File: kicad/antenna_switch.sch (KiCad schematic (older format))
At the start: 138 parts, among them K1 Fujitsu_FTR-K1C, K10 Fujitsu_FTR-K1C, K11 Fujitsu_FTR-K1C, K12 Fujitsu_FTR-K1C, K13 Fujitsu_FTR-K1C, K14 Fujitsu_FTR-K1C, K15 Fujitsu_FTR-K1C, K16 Fujitsu_FTR-K1C, K17 Fujitsu_FTR-K1C, K18 Fujitsu_FTR-K1C, K19 Fujitsu_FTR-K1C, K2 Fujitsu_FTR-K1C, K20 Fujitsu_FTR-K1C, K3 Fujitsu_FTR-K1C, K4 Fujitsu_FTR-K1C, K5 Fujitsu_FTR-K1C, K6 Fujitsu_FTR-K1C, K7 Fujitsu_FTR-K1C, K8 Fujitsu_FTR-K1C, K9 Fujitsu_FTR-K1C, Q1 BSS138, Q10 BSS138, Q11 BSS138, Q12 BSS138, Q13 BSS138, Q14 BSS138, Q15 BSS138, Q16 BSS138, Q17 BSS138, Q18 BSS138, Q19 BSS138, Q2 BSS138, Q20 BSS138, Q3 BSS138, Q4 BSS138, Q5 BSS138, Q6 BSS138, Q7 BSS138, Q8 BSS138, Q9 BSS138, U1 7400, U2 7400, U3 7400, U4 7400, U5 7400, U6 7400, U7 7400, U8 7400

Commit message: Schematic libs
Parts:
- K1, K10, K11, K12, K13, K14, K15, K16, K17, K18, K19, K2, K20, K3, K4, K5, K6, K7, K8, K9: symbol antenna_switch-rescue:Fujitsu_FTR-K1C-QS_RF -> antenna_switch:Fujitsu_FTR-K1C
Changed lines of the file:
@@
 $EndDescr
 $Comp
-L antenna_switch-rescue:Fujitsu_FTR-K1C-QS_RF K1
+L antenna_switch:Fujitsu_FTR-K1C K1
 U 1 1 5D35D937
 P 2750 1750
@@
 	2350 2100 2350 2150
 $Comp
-L antenna_switch-rescue:Fujitsu_FTR-K1C-QS_RF K2
+L antenna_switch:Fujitsu_FTR-K1C K2
 U 1 1 5D37821A
 P 2750 3800
@@
 	2350 4150 2350 4200
 $Comp
-L antenna_switch-rescue:Fujitsu_FTR-K1C-QS_RF K3
+L antenna_switch:Fujitsu_FTR-K1C K3
 U 1 1 5D37A38D
 P 2750 5900
@@
 	2000 6500 1950 6500
 $Comp
-L antenna_switch-rescue:Fujitsu_FTR-K1C-QS_RF K4
+L antenna_switch:Fujitsu_FTR-K1C K4
 U 1 1 5D3DAF7C
 P 4450 1750
@@
 	4050 2100 4050 2150
 $Comp
-L antenna_switch-rescue:Fujitsu_FTR-K1C-QS_RF K5
+L antenna_switch:Fujitsu_FTR-K1C K5
 U 1 1 5D3DAFB0
 P 4450 3800
@@
 	4050 4150 4050 4200
 $Comp
-L antenna_switch-rescue:Fujitsu_FTR-K1C-QS_RF K6
+L antenna_switch:Fujitsu_FTR-K1C K6
 U 1 1 5D3DAFD8
 P 4450 5900
@@
 	3700 6500 3650 6500
 $Comp
-L antenna_switch-rescue:Fujitsu_FTR-K1C-QS_RF K7
+L antenna_switch:Fujitsu_FTR-K1C K7
 U 1 1 5D3EC9E1
 P 6150 1750
@@
 	5750 2100 5750 2150
 $Comp
-L antenna_switch-rescue:Fujitsu_FTR-K1C-QS_RF K8
+L antenna_switch:Fujitsu_FTR-K1C K8
 U 1 1 5D3ECA15
 P 6150 3800
@@
 	5750 4150 5750 4200
 $Comp
-L antenna_switch-rescue:Fujitsu_FTR-K1C-QS_RF K9
+L antenna_switch:Fujitsu_FTR-K1C K9
 U 1 1 5D3ECA3D
 P 6150 5900
@@
 	5400 6500 5350 6500
 $Comp
-L antenna_switch-rescue:Fujitsu_FTR-K1C-QS_RF K10
+L antenna_switch:Fujitsu_FTR-K1C K10
 U 1 1 5D437770
 P 7850 1750
@@
 	7450 2100 7450 2150
 $Comp
-L antenna_switch-rescue:Fujitsu_FTR-K1C-QS_RF K11
+L antenna_switch:Fujitsu_FTR-K1C K11
 U 1 1 5D4377A4
 P 7850 3800
@@
 	7450 4150 7450 4200
 $Comp
-L antenna_switch-rescue:Fujitsu_FTR-K1C-QS_RF K12
+L antenna_switch:Fujitsu_FTR-K1C K12
 U 1 1 5D4377CC
 P 7850 5900
@@
 	7100 6500 7050 6500
 $Comp
-L antenna_switch-rescue:Fujitsu_FTR-K1C-QS_RF K13
+L antenna_switch:Fujitsu_FTR-K1C K13
 U 1 1 5D437834
 P 9550 1750
@@
 	9150 2100 9150 2150
 $Comp
-L antenna_switch-rescue:Fujitsu_FTR-K1C-QS_RF K14
+L antenna_switch:Fujitsu_FTR-K1C K14
 U 1 1 5D437868
 P 9550 3800
@@
 	9150 4150 9150 4200
 $Comp
-L antenna_switch-rescue:Fujitsu_FTR-K1C-QS_RF K15
+L antenna_switch:Fujitsu_FTR-K1C K15
 U 1 1 5D437890
 P 9550 5900
@@
 	8800 6500 8750 6500
 $Comp
-L antenna_switch-rescue:Fujitsu_FTR-K1C-QS_RF K16
+L antenna_switch:Fujitsu_FTR-K1C K16
 U 1 1 5D4378F8
 P 11250 1750
@@
 	10850 2100 10850 2150
 $Comp
-L antenna_switch-rescue:Fujitsu_FTR-K1C-QS_RF K17
+L antenna_switch:Fujitsu_FTR-K1C K17
 U 1 1 5D43792C
 P 11250 3800
@@
 	10850 4150 10850 4200
 $Comp
-L antenna_switch-rescue:Fujitsu_FTR-K1C-QS_RF K18
+L antenna_switch:Fujitsu_FTR-K1C K18
 U 1 1 5D437954
 P 11250 5900
@@
 $EndComp
 $Comp
-L antenna_switch-rescue:Fujitsu_FTR-K1C-QS_RF K19
+L antenna_switch:Fujitsu_FTR-K1C K19
 U 1 1 5D67F737
 P 12750 2350
@@
 Connection ~ 11400 3050
 $Comp
-L antenna_switch-rescue:Fujitsu_FTR-K1C-QS_RF K20
+L antenna_switch:Fujitsu_FTR-K1C K20
 U 1 1 5DD9CFD4
 P 12750 4650

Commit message: Compensation coils
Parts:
- added L1, L2: L, symbol Device:L
- gave numbers to parts that had none: 8
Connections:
- wire segments 530 -> 532

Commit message: Relays in series to increase isolation
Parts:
- removed C8: 100n, symbol Device:C_Small
- removed D10, D11, D12, D14, D15, D16, D4, D6, D7, D8, D9: 1N4148WS, Diode_SMD:D_SOD-323, symbol Diode:1N4148WS
- removed EXT1, EXT2, LOAD1, LOAD2, RADIO1, RADIO2: Conn_Coaxial, symbol Connector:Conn_Coaxial
- removed K19, K20, K4, K6: Fujitsu_FTR-K1C, QS_RF:Relay_DPDT_Fujitsu_FTR-K1C, symbol antenna_switch:Fujitsu_FTR-K1C
- removed L1, L2: L, symbol Device:L
- removed Q1, Q10, Q11, Q12, Q13, Q14, Q15, Q16, Q17, Q18, Q19, Q2, Q20, Q3, Q4, Q5, Q6, Q7, Q8, Q9: BSS138, Package_TO_SOT_SMD:SOT-23, symbol Transistor_FET:BSS138
- removed R1, R10, R11, R12, R13, R14, R15, R16, R17, R18, R19, R2, R20, R3, R4, R5, R6, R7, R8, R9: 470k, symbol Device:R_Small
- removed U1, U10, U11, U12, U13, U14, U15, U16, U2, U3, U4, U5, U6, U7, U8, U9: 7400, symbol 74xx:7400
- added C10, C11, C12, C13, C14, C9: 1n, symbol Device:C_Small
- added C8: 470u, symbol Device:CP_Small
- added D1, D10, D15, D16, D2, D24, D25, D30, D31, D38, D39, D9: CGA0603MLC-12E, symbol Device:D_TVS
- added D11, D12, D21, D22, D23, D26, D27, D36, D37, D40, D41, D7, D8: LED, symbol Device:LED
- added D28, D29, D3, D32, D33, D34, D35, D42, D43: 1N4148WS, Diode_SMD:D_SOD-323, symbol Diode:1N4148WS
- added E1, E10, E13, E14, E15, E16, E17, E2, E3, E4, E7, E8, E9: CG775MS, symbol Device:SPARK_GAP
- added E11, E12, E18, E19, E5, E6: SL1002A600SM, symbol Device:SPARK_GAP
- added J1: Conn_02x07_Odd_Even, symbol Connector_Generic:Conn_02x07_Odd_Even
- added J2: Conn_01x02, symbol Connector_Generic:Conn_01x02
- added K1, K3: Fujitsu_FTR-K1C, QS_RF:Relay_DPDT_Fujitsu_FTR-K1C, symbol antenna_switch:Fujitsu_FTR-K1C
- added L1, L2: L_Small, symbol Device:L_Small
- added Q1, Q10, Q11, Q12, Q2, Q3, Q4, Q5, Q6, Q7, Q8, Q9: BC817, Package_TO_SOT_SMD:SOT-23, symbol Transistor_BJT:BC817
- added R1, R10, R13, R14, R2, R22, R23, R26, R27, R34, R35, R9: 1k, symbol Device:R
- added R11, R12, R19, R20, R21, R24, R25, R32, R33, R36, R37, R7, R8: 4.7k, symbol Device:R
- added R15, R16, R17, R18, R28, R29, R3, R30, R31, R4, R5, R6: 100, symbol Device:R
- added TRX1, TRX2: Conn_Coaxial, symbol Connector:Conn_Coaxial
- C1, C2, C3, C4, C5, C6: value 100n -> 1n
- renumbered D3 to D14, D2 to D4, D1 to D6, K1 to K4, K3 to K6
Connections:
- net labels added: RADIO_1, RADIO_2
- net labels removed: Rel_A1G, Rel_A1R1, Rel_A1R2, Rel_A2G, Rel_A2R1, Rel_A2R2, Rel_A3G, Rel_A3R1, Rel_A3R2, Rel_A4G, Rel_A4R1, Rel_A4R2, Rel_A5G, Rel_A5R1, Rel_A5R2, Rel_A6G, Rel_A6R1, Rel_A6R2, Rel_R1L, Rel_R2L
- wire segments 532 -> 459
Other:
- moved on the sheet: A1, D14, D4, D6, K2, K4, K6

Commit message: Initial PCB layout work
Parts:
- removed E1, E10, E13, E14, E15, E16, E17, E2, E3, E4, E9: CG775MS, symbol Device:SPARK_GAP
- added D30: TESDU24V, Resistor_SMD:R_0603_1608Metric_Pad1.05x0.95mm_HandSolder, symbol Device:D_TVS
- added F1: 0ZCJ0025AF2E, Fuse:Fuse_1206_3216Metric_Pad1.42x1.75mm_HandSolder, symbol Device:Polyfuse_Small
- A1, A2, A3, A4, A5, A6, TRX1, TRX2: footprint (none) -> QS_RF:UC1-Square-2HolesRight
- C1: renamed from C2; footprint (none) -> Capacitor_SMD:C_0805_2012Metric_Pad1.15x1.40mm_HandSolder
- C10: renamed from C9; footprint (none) -> Capacitor_SMD:C_0805_2012Metric_Pad1.15x1.40mm_HandSolder
- C11: renamed from C12; footprint (none) -> Capacitor_SMD:C_0805_2012Metric_Pad1.15x1.40mm_HandSolder
- C12: renamed from C11; footprint (none) -> Capacitor_SMD:C_0805_2012Metric_Pad1.15x1.40mm_HandSolder
- C13: renamed from C14; footprint (none) -> Capacitor_SMD:C_0805_2012Metric_Pad1.15x1.40mm_HandSolder
- C14: renamed from C13; footprint (none) -> Capacitor_SMD:C_0805_2012Metric_Pad1.15x1.40mm_HandSolder
- C2: renamed from C1; footprint (none) -> Capacitor_SMD:C_0805_2012Metric_Pad1.15x1.40mm_HandSolder
- C3: renamed from C4; footprint (none) -> Capacitor_SMD:C_0805_2012Metric_Pad1.15x1.40mm_HandSolder
- C4: renamed from C3; footprint (none) -> Capacitor_SMD:C_0805_2012Metric_Pad1.15x1.40mm_HandSolder
- C5: renamed from C6; footprint (none) -> Capacitor_SMD:C_0805_2012Metric_Pad1.15x1.40mm_HandSolder
- C6: renamed from C5; footprint (none) -> Capacitor_SMD:C_0805_2012Metric_Pad1.15x1.40mm_HandSolder
- C7: footprint (none) -> Capacitor_SMD:C_0805_2012Metric_Pad1.15x1.40mm_HandSolder
- C8: footprint (none) -> Capacitor_THT:CP_Radial_D8.0mm_P3.50mm
- C9: renamed from C10; footprint (none) -> Capacitor_SMD:C_0805_2012Metric_Pad1.15x1.40mm_HandSolder
- D1: renamed from D2; value CGA0603MLC-12E -> TESDU24V; footprint (none) -> Resistor_SMD:R_0603_1608Metric_Pad1.05x0.95mm_HandSolder
- D10: renamed from D9; value CGA0603MLC-12E -> TESDU24V; footprint (none) -> Resistor_SMD:R_0603_1608Metric_Pad1.05x0.95mm_HandSolder
- D11: renamed from D12; footprint (none) -> LED_SMD:LED_0805_2012Metric_Pad1.15x1.40mm_HandSolder
- D12: renamed from D11; footprint (none) -> LED_SMD:LED_0805_2012Metric_Pad1.15x1.40mm_HandSolder
- D15: renamed from D16; value CGA0603MLC-12E -> TESDU24V; footprint (none) -> Resistor_SMD:R_0603_1608Metric_Pad1.05x0.95mm_HandSolder
- D16: renamed from D15; value CGA0603MLC-12E -> TESDU24V; footprint (none) -> Resistor_SMD:R_0603_1608Metric_Pad1.05x0.95mm_HandSolder
- D2: renamed from D1; value CGA0603MLC-12E -> TESDU24V; footprint (none) -> Resistor_SMD:R_0603_1608Metric_Pad1.05x0.95mm_HandSolder
- D21: renamed from D22; footprint (none) -> LED_SMD:LED_0805_2012Metric_Pad1.15x1.40mm_HandSolder
- D22: renamed from D21; footprint (none) -> LED_SMD:LED_0805_2012Metric_Pad1.15x1.40mm_HandSolder
- D23, D37, D41: footprint (none) -> LED_SMD:LED_0805_2012Metric_Pad1.15x1.40mm_HandSolder
- D24: renamed from D25; value CGA0603MLC-12E -> TESDU24V; footprint (none) -> Resistor_SMD:R_0603_1608Metric_Pad1.05x0.95mm_HandSolder
- D25: renamed from D24; value CGA0603MLC-12E -> TESDU24V; footprint (none) -> Resistor_SMD:R_0603_1608Metric_Pad1.05x0.95mm_HandSolder
- D26: renamed from D27; footprint (none) -> LED_SMD:LED_0805_2012Metric_Pad1.15x1.40mm_HandSolder
- D27: renamed from D26; footprint (none) -> LED_SMD:LED_0805_2012Metric_Pad1.15x1.40mm_HandSolder
- D31, D39: value CGA0603MLC-12E -> TESDU24V; footprint (none) -> Resistor_SMD:R_0603_1608Metric_Pad1.05x0.95mm_HandSolder
- D32: renamed from D30; value CGA0603MLC-12E -> TESDU24V; footprint (none) -> Resistor_SMD:R_0603_1608Metric_Pad1.05x0.95mm_HandSolder
- D38: renamed from D36; footprint (none) -> LED_SMD:LED_0805_2012Metric_Pad1.15x1.40mm_HandSolder
- D40: renamed from D38; value CGA0603MLC-12E -> TESDU24V; footprint (none) -> Resistor_SMD:R_0603_1608Metric_Pad1.05x0.95mm_HandSolder
- D42: renamed from D40; footprint (none) -> LED_SMD:LED_0805_2012Metric_Pad1.15x1.40mm_HandSolder
- D7: renamed from D8; footprint (none) -> LED_SMD:LED_0805_2012Metric_Pad1.15x1.40mm_HandSolder
- D8: renamed from D7; footprint (none) -> LED_SMD:LED_0805_2012Metric_Pad1.15x1.40mm_HandSolder
- D9: renamed from D10; value CGA0603MLC-12E -> TESDU24V; footprint (none) -> Resistor_SMD:R_0603_1608Metric_Pad1.05x0.95mm_HandSolder
- E1: renamed from E6; footprint (none) -> QS_RF:GDT_SL1002A_HandSolder
- E2: renamed from E5; footprint (none) -> QS_RF:GDT_SL1002A_HandSolder
- E3: renamed from E12; footprint (none) -> QS_RF:GDT_SL1002A_HandSolder
- E4: renamed from E11; footprint (none) -> QS_RF:GDT_SL1002A_HandSolder
- E5: renamed from E19; footprint (none) -> QS_RF:GDT_SL1002A_HandSolder
- E6: renamed from E18; footprint (none) -> QS_RF:GDT_SL1002A_HandSolder
- E7, E8: value CG775MS -> SL1002A600SM; footprint (none) -> QS_RF:GDT_SL1002A_HandSolder
- J1: footprint (none) -> Connector_IDC:IDC-Header_2x07_P2.54mm_Vertical
- J2: footprint (none) -> TerminalBlock:TerminalBlock_bornier-2_P5.08mm
- L1, L2: footprint (none) -> Inductor_THT:L_Axial_L13.0mm_D4.5mm_P15.24mm_Horizontal_Fastron_HCCC
- R1: renamed from R2; footprint (none) -> Resistor_SMD:R_0805_2012Metric_Pad1.15x1.40mm_HandSolder
- R10: renamed from R9; footprint (none) -> Resistor_SMD:R_0805_2012Metric_Pad1.15x1.40mm_HandSolder
- R11: renamed from R12; footprint (none) -> Resistor_SMD:R_0805_2012Metric_Pad1.15x1.40mm_HandSolder
- R12: renamed from R11; footprint (none) -> Resistor_SMD:R_0805_2012Metric_Pad1.15x1.40mm_HandSolder
- R13: renamed from R14; footprint (none) -> Resistor_SMD:R_0805_2012Metric_Pad1.15x1.40mm_HandSolder
- R14: renamed from R13; footprint (none) -> Resistor_SMD:R_0805_2012Metric_Pad1.15x1.40mm_HandSolder
- R15: renamed from R16; footprint (none) -> Resistor_SMD:R_2512_6332Metric_Pad1.52x3.35mm_HandSolder
- R16: renamed from R15; footprint (none) -> Resistor_SMD:R_2512_6332Metric_Pad1.52x3.35mm_HandSolder
- R17: renamed from R18; footprint (none) -> Resistor_SMD:R_2512_6332Metric_Pad1.52x3.35mm_HandSolder
- R18: renamed from R17; footprint (none) -> Resistor_SMD:R_2512_6332Metric_Pad1.52x3.35mm_HandSolder
- R19: renamed from R20; footprint (none) -> Resistor_SMD:R_0805_2012Metric_Pad1.15x1.40mm_HandSolder
- R2: renamed from R1; footprint (none) -> Resistor_SMD:R_0805_2012Metric_Pad1.15x1.40mm_HandSolder
- R20: renamed from R19; footprint (none) -> Resistor_SMD:R_0805_2012Metric_Pad1.15x1.40mm_HandSolder
- R21: footprint (none) -> Resistor_SMD:R_0805_2012Metric_Pad1.15x1.40mm_HandSolder
- R22: renamed from R23; footprint (none) -> Resistor_SMD:R_0805_2012Metric_Pad1.15x1.40mm_HandSolder
- R23: renamed from R22; footprint (none) -> Resistor_SMD:R_0805_2012Metric_Pad1.15x1.40mm_HandSolder
- R24: renamed from R25; footprint (none) -> Resistor_SMD:R_0805_2012Metric_Pad1.15x1.40mm_HandSolder
- R25: renamed from R24; footprint (none) -> Resistor_SMD:R_0805_2012Metric_Pad1.15x1.40mm_HandSolder
- R26: renamed from R27; footprint (none) -> Resistor_SMD:R_0805_2012Metric_Pad1.15x1.40mm_HandSolder
- R27: renamed from R26; footprint (none) -> Resistor_SMD:R_0805_2012Metric_Pad1.15x1.40mm_HandSolder
- R28: renamed from R29; footprint (none) -> Resistor_SMD:R_2512_6332Metric_Pad1.52x3.35mm_HandSolder
- R29: renamed from R28; footprint (none) -> Resistor_SMD:R_2512_6332Metric_Pad1.52x3.35mm_HandSolder
- R3: renamed from R4; footprint (none) -> Resistor_SMD:R_2512_6332Metric_Pad1.52x3.35mm_HandSolder
- R30: renamed from R31; footprint (none) -> Resistor_SMD:R_2512_6332Metric_Pad1.52x3.35mm_HandSolder
- R31: renamed from R30; footprint (none) -> Resistor_SMD:R_2512_6332Metric_Pad1.52x3.35mm_HandSolder
- R32: renamed from R33; footprint (none) -> Resistor_SMD:R_0805_2012Metric_Pad1.15x1.40mm_HandSolder
- R33: renamed from R32; footprint (none) -> Resistor_SMD:R_0805_2012Metric_Pad1.15x1.40mm_HandSolder
- R34: renamed from R35; footprint (none) -> Resistor_SMD:R_0805_2012Metric_Pad1.15x1.40mm_HandSolder
- R35: renamed from R34; footprint (none) -> Resistor_SMD:R_0805_2012Metric_Pad1.15x1.40mm_HandSolder
- R36: renamed from R37; footprint (none) -> Resistor_SMD:R_0805_2012Metric_Pad1.15x1.40mm_HandSolder
- R37: renamed from R36; footprint (none) -> Resistor_SMD:R_0805_2012Metric_Pad1.15x1.40mm_HandSolder
- R4: renamed from R3; footprint (none) -> Resistor_SMD:R_2512_6332Metric_Pad1.52x3.35mm_HandSolder
- R5: renamed from R6; footprint (none) -> Resistor_SMD:R_2512_6332Metric_Pad1.52x3.35mm_HandSolder
- R6: renamed from R5; footprint (none) -> Resistor_SMD:R_2512_6332Metric_Pad1.52x3.35mm_HandSolder
- R7: renamed from R8; footprint (none) -> Resistor_SMD:R_0805_2012Metric_Pad1.15x1.40mm_HandSolder
- R8: renamed from R7; footprint (none) -> Resistor_SMD:R_0805_2012Metric_Pad1.15x1.40mm_HandSolder
- R9: renamed from R10; footprint (none) -> Resistor_SMD:R_0805_2012Metric_Pad1.15x1.40mm_HandSolder
- renumbered D14 to D13, D13 to D14, D18 to D17, D17 to D18, D20 to D19, D19 to D20, D29 to D28, D28 to D29, D4 to D3, D32 to D34, D34 to D36, D3 to D4, D42 to D44, D6 to D5, D5 to D6, K2 to K1, K9 to K10, K12 to K11, K11 to K12, K14 to K13, K13 to K14, K16 to K15, K15 to K16, K18 to K17, K17 to K18, K1 to K2, K4 to K3, K3 to K4, K6 to K5, K5 to K6, K8 to K7, K7 to K8, K10 to K9, Q2 to Q1, Q9 to Q10, Q12 to Q11, Q11 to Q12, Q1 to Q2, Q4 to Q3, Q3 to Q4, Q6 to Q5, Q5 to Q6, Q8 to Q7, Q7 to Q8, Q10 to Q9
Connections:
- net +12V: now also D30.1 (A1), F1.2; no longer J2.1 (Pin_1)
- net A2R1: no longer E8.2
- net A5R1: no longer E7.2
- net GND: now also E7.2, E8.2, D30.2 (A2); no longer E7.1, E8.1
- net RADIO_1: now also E7.1
- net RADIO_2: now also E8.1
- new net: F1.1, J2.1 (Pin_1)
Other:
- moved on the sheet: A4, A5, A6, C10, C12, C14, C2, C4, C6, D10, D12, D14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

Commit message: Some more layout
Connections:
- net RADIO_1: no longer E7.1
- net RADIO_2: no longer E8.1
- net at L1.2, TRX1.1 (In): now also E7.1
- net at L2.2, TRX2.1 (In): now also E8.1
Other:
- moved on the sheet: E7, E8, L1, L2
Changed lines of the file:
@@
 L Device:L_Small L1
 U 1 1 5F303E6A
-P 14700 4250
-F 0 "L1" V 14793 4250 50  0000 C CNN
-F 1 "L_Small" V 14794 4250 50  0001 C CNN
-F 2 "Inductor_THT:L_Axial_L13.0mm_D4.5mm_P15.24mm_Horizontal_Fastron_HCCC" H 14700 4250 50  0001 C CNN
-F 3 "~" H 14700 4250 50  0001 C CNN
-	1    14700 4250
+P 14650 4250
+F 0 "L1" V 14743 4250 50  0000 C CNN
+F 1 "L_Small" V 14744 4250 50  0001 C CNN
+F 2 "Inductor_THT:L_Axial_L13.0mm_D4.5mm_P15.24mm_Horizontal_Fastron_HCCC" H 14650 4250 50  0001 C CNN
+F 3 "~" H 14650 4250 50  0001 C CNN
+	1    14650 4250
 	0    -1   -1   0
 $EndComp
 Wire Wire Line
-	14300 4250 14500 4250
-Wire Wire Line
-	14800 4250 14850 4250
+	14750 4250 14800 4250
 $Comp
 L power:GND #PWR079
@@
 L Device:L_Small L2
 U 1 1 5F367006
-P 14700 5250
-F 0 "L2" V 14793 5250 50  0000 C CNN
-F 1 "L_Small" V 14794 5250 50  0001 C CNN
-F 2 "Inductor_THT:L_Axial_L13.0mm_D4.5mm_P15.24mm_Horizontal_Fastron_HCCC" H 14700 5250 50  0001 C CNN
-F 3 "~" H 14700 5250 50  0001 C CNN
-	1    14700 5250
+P 14650 5250
+F 0 "L2" V 14743 5250 50  0000 C CNN
+F 1 "L_Small" V 14744 5250 50  0001 C CNN
+F 2 "Inductor_THT:L_Axial_L13.0mm_D4.5mm_P15.24mm_Horizontal_Fastron_HCCC" H 14650 5250 50  0001 C CNN
+F 3 "~" H 14650 5250 50  0001 C CNN
+	1    14650 5250
 	0    -1   -1   0
 $EndComp
 Wire Wire Line
-	14300 5250 14500 5250
-Wire Wire Line
-	14800 5250 14850 5250
+	14750 5250 14800 5250
 $Comp
 L power:GND #PWR080
@@
 L Device:SPARK_GAP E7
 U 1 1 5FEAD585
-P 14500 4450
-F 0 "E7" H 14550 4550 50  0000 R CNN
-F 1 "SL1002A600SM" H 14500 4350 50  0000 C CNN
-F 2 "QS_RF:GDT_SL1002A_HandSolder" H 14500 4380 50  0001 C CNN
-F 3 "~" V 14500 4450 50  0001 C CNN
-	1    14500 4450
-	0    1    1    0
-$EndComp
-Connection ~ 14500 4250
-Wire Wire Line
-	14500 4250 14600 4250
+P 14800 4450
+F 0 "E7" H 14850 4550 50  0000 R CNN
+F 1 "SL1002A600SM" H 14800 4350 50  0000 C CNN
+F 2 "QS_RF:GDT_SL1002A_HandSolder" H 14800 4380 50  0001 C CNN
+F 3 "~" V 14800 4450 50  0001 C CNN
+	1    14800 4450
+	0    1    1    0
+$EndComp
 $Comp
 L Device:SPARK_GAP E8
 U 1 1 5FEAE9F8
-P 14500 5450
-F 0 "E8" H 14550 5550 50  0000 R CNN
-F 1 "SL1002A600SM" H 14500 5350 50  0000 C CNN
-F 2 "QS_RF:GDT_SL1002A_HandSolder" H 14500 5380 50  0001 C CNN
-F 3 "~" V 14500 5450 50  0001 C CNN
-	1    14500 5450
-	0    1    1    0
-$EndComp
-Connection ~ 14500 5250
-Wire Wire Line
-	14500 5250 14600 5250
+P 14800 5450
+F 0 "E8" H 14850 5550 50  0000 R CNN
+F 1 "SL1002A600SM" H 14800 5350 50  0000 C CNN
+F 2 "QS_RF:GDT_SL1002A_HandSolder" H 14800 5380 50  0001 C CNN
+F 3 "~" V 14800 5450 50  0001 C CNN
+	1    14800 5450
+	0    1    1    0
+$EndComp
 $Comp
 L power:GND #PWR077
 U 1 1 5FEAF0D0
-P 14500 4650
-F 0 "#PWR077" H 14500 4400 50  0001 C CNN
-F 1 "GND" H 14505 4477 50  0000 C CNN
-F 2 "" H 14500 4650 50  0001 C CNN
-F 3 "" H 14500 4650 50  0001 C CNN
-	1    14500 4650
+P 14800 4650
+F 0 "#PWR077" H 14800 4400 50  0001 C CNN
+F 1 "GND" H 14805 4477 50  0000 C CNN
+F 2 "" H 14800 4650 50  0001 C CNN
+F 3 "" H 14800 4650 50  0001 C CNN
+	1    14800 4650
 	1    0    0    -1
 $EndComp
@@
 L power:GND #PWR078
 U 1 1 5FEAF70E
-P 14500 5650
-F 0 "#PWR078" H 14500 5400 50  0001 C CNN
-F 1 "GND" H 14505 5477 50  0000 C CNN
-F 2 "" H 14500 5650 50  0001 C CNN
-F 3 "" H 14500 5650 50  0001 C CNN
-	1    14500 5650
+P 14800 5650
+F 0 "#PWR078" H 14800 5400 50  0001 C CNN
+F 1 "GND" H 14805 5477 50  0000 C CNN
+F 2 "" H 14800 5650 50  0001 C CNN
+F 3 "" H 14800 5650 50  0001 C CNN
+	1    14800 5650
 	1    0    0    -1
 $EndComp
@@
 Wire Wire Line
 	8550 9700 8850 9700
+Wire Wire Line
+	14300 4250 14550 4250
+Connection ~ 14800 4250
+Wire Wire Line
+	14800 4250 14850 4250
+Connection ~ 14800 5250
+Wire Wire Line
+	14800 5250 14850 5250
+Wire Wire Line
+	14300 5250 14550 5250
 $EndSCHEMATC

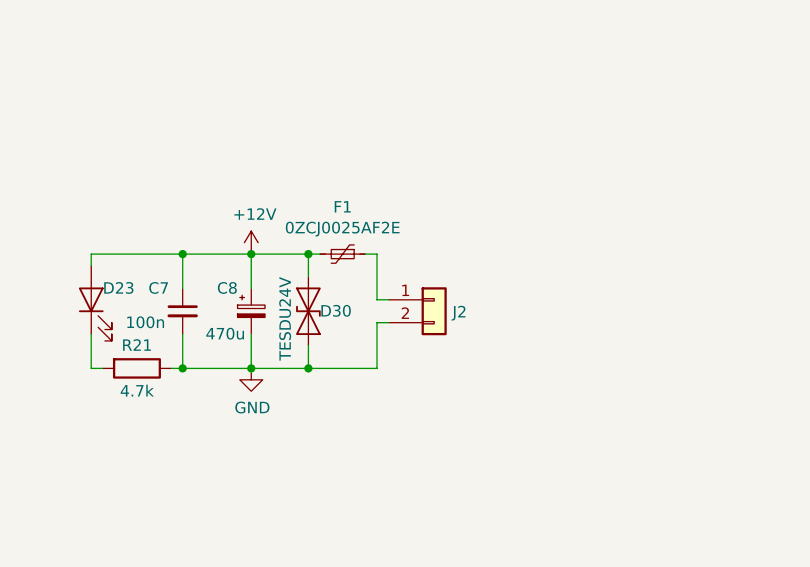
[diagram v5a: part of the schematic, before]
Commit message: reverse protection diode
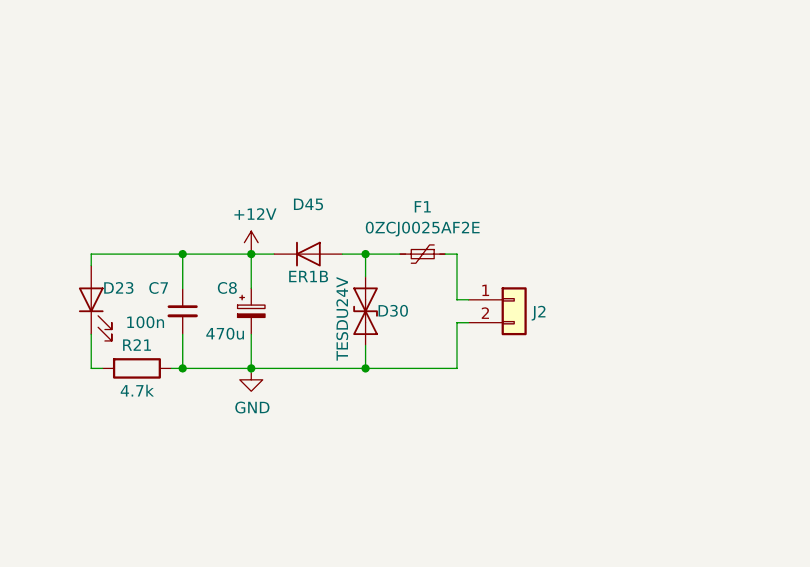
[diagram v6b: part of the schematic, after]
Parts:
- added D45: ER1B, Diode_SMD:D_SMA_Handsoldering, symbol Device:D
- L1, L2: footprint Inductor_THT:L_Axial_L13.0mm_D4.5mm_P15.24mm_Horizontal_Fastron_HCCC -> Resistor_THT:R_Axial_DIN0411_L9.9mm_D3.6mm_P12.70mm_Horizontal
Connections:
- net +12V: now also D45.1 (K); no longer D30.1 (A1), F1.2
- new net: D30.1 (A1), D45.2 (A), F1.2
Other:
- moved on the sheet: D30, F1, J2
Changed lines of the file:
@@
 L Connector_Generic:Conn_01x02 J2
 U 1 1 5EDD88BF
-P 9100 9400
-F 0 "J2" H 9180 9346 50  0000 L CNN
-F 1 "Conn_01x02" H 9180 9301 50  0001 L CNN
-F 2 "TerminalBlock:TerminalBlock_bornier-2_P5.08mm" H 9100 9400 50  0001 C CNN
-F 3 "~" H 9100 9400 50  0001 C CNN
-	1    9100 9400
+P 9450 9400
+F 0 "J2" H 9530 9346 50  0000 L CNN
+F 1 "Conn_01x02" H 9530 9301 50  0001 L CNN
+F 2 "TerminalBlock:TerminalBlock_bornier-2_P5.08mm" H 9450 9400 50  0001 C CNN
+F 3 "~" H 9450 9400 50  0001 C CNN
+	1    9450 9400
 	1    0    0    -1
 $EndComp
@@
 F 0 "L1" V 14743 4250 50  0000 C CNN
 F 1 "L_Small" V 14744 4250 50  0001 C CNN
-F 2 "Inductor_THT:L_Axial_L13.0mm_D4.5mm_P15.24mm_Horizontal_Fastron_HCCC" H 14650 4250 50  0001 C CNN
+F 2 "Resistor_THT:R_Axial_DIN0411_L9.9mm_D3.6mm_P12.70mm_Horizontal" H 14650 4250 50  0001 C CNN
 F 3 "~" H 14650 4250 50  0001 C CNN
 	1    14650 4250
@@
 F 0 "L2" V 14743 5250 50  0000 C CNN
 F 1 "L_Small" V 14744 5250 50  0001 C CNN
-F 2 "Inductor_THT:L_Axial_L13.0mm_D4.5mm_P15.24mm_Horizontal_Fastron_HCCC" H 14650 5250 50  0001 C CNN
+F 2 "Resistor_THT:R_Axial_DIN0411_L9.9mm_D3.6mm_P12.70mm_Horizontal" H 14650 5250 50  0001 C CNN
 F 3 "~" H 14650 5250 50  0001 C CNN
 	1    14650 5250
@@
 $EndComp
 Wire Wire Line
-	8600 9200 8550 9200
-Connection ~ 8550 9700
-Connection ~ 8550 9200
-Wire Wire Line
-	8550 9200 8300 9200
-Wire Wire Line
 	8000 9200 8000 9350
 Wire Wire Line
@@
 	8300 9200 8000 9200
 Wire Wire Line
-	8550 9700 8300 9700
-Wire Wire Line
 	8300 9700 8300 9550
 Wire Wire Line
@@
 L Device:D_TVS D30
 U 1 1 5FD5962E
-P 8550 9450
-F 0 "D30" V 8550 9500 50  0000 L CNN
-F 1 "TESDU24V" H 8400 9350 50  0000 L CNN
-F 2 "Resistor_SMD:R_0603_1608Metric_Pad1.05x0.95mm_HandSolder" H 8550 9450 50  0001 C CNN
-F 3 "~" H 8550 9450 50  0001 C CNN
-	1    8550 9450
+P 8800 9450
+F 0 "D30" V 8800 9500 50  0000 L CNN
+F 1 "TESDU24V" H 8650 9350 50  0000 L CNN
+F 2 "Resistor_SMD:R_0603_1608Metric_Pad1.05x0.95mm_HandSolder" H 8800 9450 50  0001 C CNN
+F 3 "~" H 8800 9450 50  0001 C CNN
+	1    8800 9450
 	0    1    1    0
 $EndComp
-Wire Wire Line
-	8550 9300 8550 9200
-Wire Wire Line
-	8550 9600 8550 9700
 $Comp
 L Device:SPARK_GAP E7
@@
 L Device:Polyfuse_Small F1
 U 1 1 60171796
-P 8700 9200
-F 0 "F1" V 8495 9200 50  0000 C CNN
-F 1 "0ZCJ0025AF2E" V 8586 9200 50  0000 C CNN
-F 2 "Fuse:Fuse_1206_3216Metric_Pad1.42x1.75mm_HandSolder" H 8750 9000 50  0001 L CNN
-F 3 "~" H 8700 9200 50  0001 C CNN
-	1    8700 9200
+P 9050 9200
+F 0 "F1" V 8845 9200 50  0000 C CNN
+F 1 "0ZCJ0025AF2E" V 8936 9200 50  0000 C CNN
+F 2 "Fuse:Fuse_1206_3216Metric_Pad1.42x1.75mm_HandSolder" H 9100 9000 50  0001 L CNN
+F 3 "~" H 9050 9200 50  0001 C CNN
+	1    9050 9200
 	0    1    1    0
 $EndComp
 Wire Wire Line
-	8800 9200 8850 9200
-Wire Wire Line
-	8850 9200 8850 9400
+	9150 9200 9200 9200
 Wire Wire Line
-	8850 9400 8900 9400
+	9200 9200 9200 9400
 Wire Wire Line
-	8900 9500 8850 9500
+	9200 9400 9250 9400
 Wire Wire Line
-	8850 9500 8850 9700
+	9250 9500 9200 9500
 Wire Wire Line
-	8550 9700 8850 9700
+	9200 9500 9200 9700
 Wire Wire Line
 	14300 4250 14550 4250
@@
 Wire Wire Line
 	14300 5250 14550 5250
+$Comp
+L Device:D D45
+U 1 1 5EC6E3C6
+P 8550 9200
+F 0 "D45" H 8550 9416 50  0000 C CNN
+F 1 "ER1B" H 8550 9100 50  0000 C CNN
+F 2 "Diode_SMD:D_SMA_Handsoldering" H 8550 9200 50  0001 C CNN
+F 3 "~" H 8550 9200 50  0001 C CNN
+	1    8550 9200
+	1    0    0    -1
+$EndComp
+Wire Wire Line
+	8700 9200 8800 9200
+Wire Wire Line
+	8300 9200 8400 9200
+Wire Wire Line
+	8300 9700 8800 9700
+Wire Wire Line
+	8800 9600 8800 9700
+Connection ~ 8800 9700
+Wire Wire Line
+	8800 9700 9200 9700
+Wire Wire Line
+	8800 9300 8800 9200
+Connection ~ 8800 9200
+Wire Wire Line
+	8800 9200 8950 9200
 $EndSCHEMATC
